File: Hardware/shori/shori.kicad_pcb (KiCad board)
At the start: 4 copper layers, 106 x 44.5 mm, 130 parts, among them J2 SWD_Header, SW1 SW_SPDT, U1 CS4272, U2 STM32H750VBTx, U3 NE5532, U4 NE5532, U5 TPS73733DCQR, U6 W25Q128JVS, U7 TLV9001IDCK, U8 MAX40200AUK, Y1 16MHz

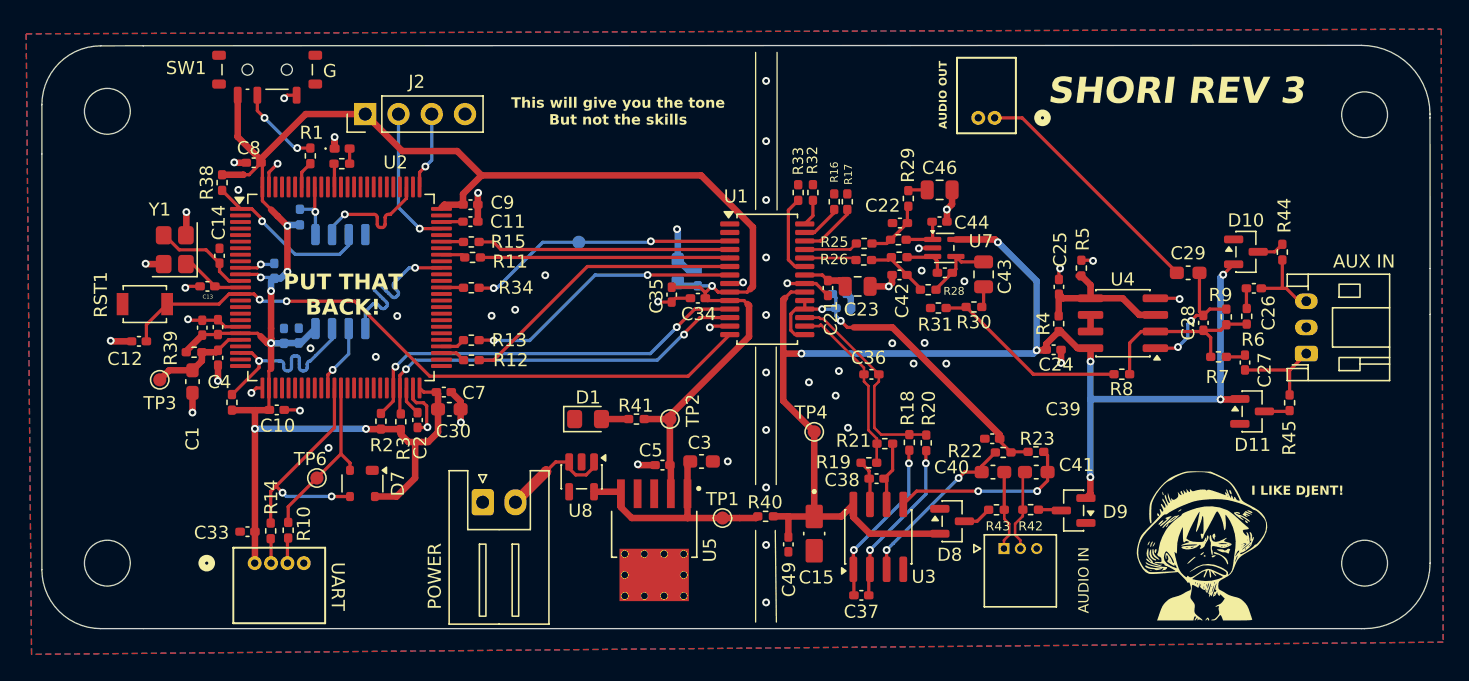
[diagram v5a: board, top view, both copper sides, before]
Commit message: Mae rev 1 schems done! power supply and audio out
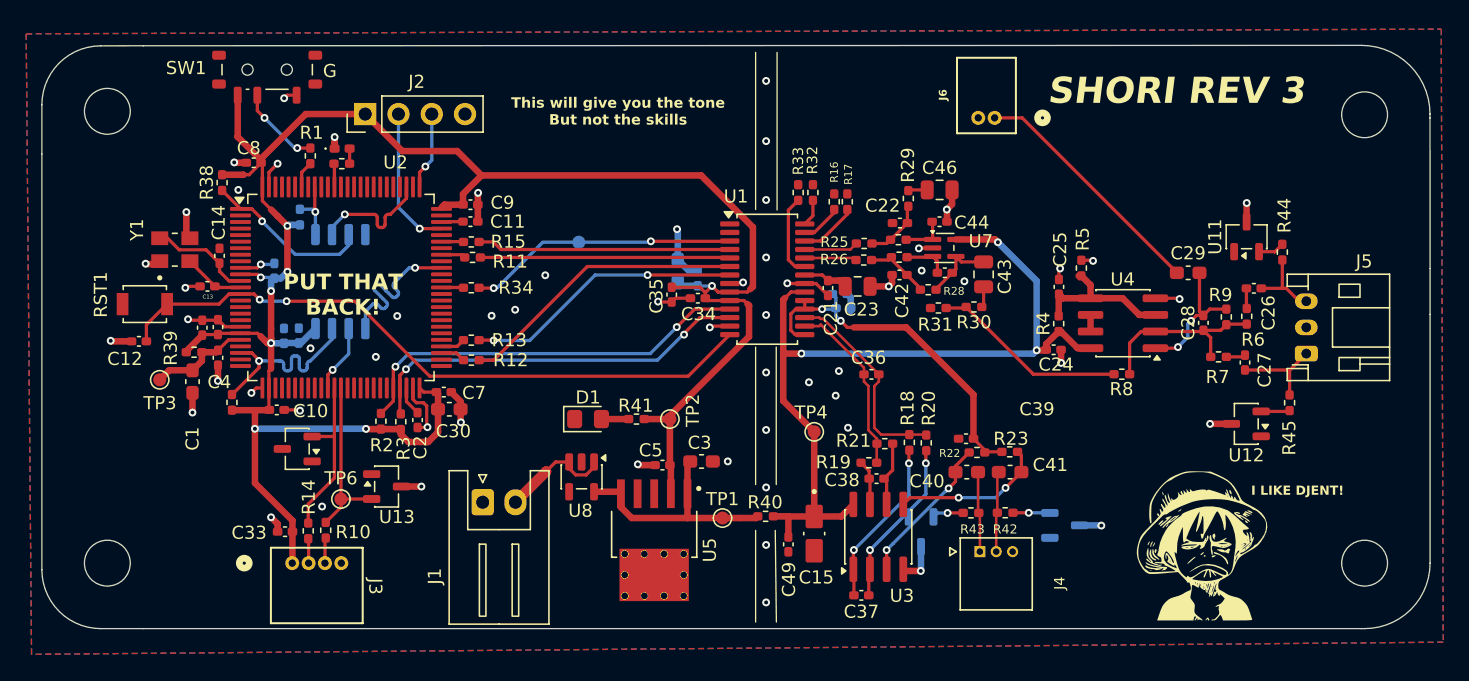
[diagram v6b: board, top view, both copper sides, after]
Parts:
- removed D10, D11, D8, D9: BAT54C, Package_TO_SOT_SMD:SOT-23
- removed D7: PRTR5V0U2X, Package_TO_SOT_SMD:SOT-143
- added U10: ~, Package_TO_SOT_SMD:SOT-23-3, B.Cu at (175.1, 127.6)
- added U11: ~, Package_TO_SOT_SMD:SOT-23-3, F.Cu at (189.0, 105.6)
- added U12: ~, Package_TO_SOT_SMD:SOT-23-3, F.Cu at (189.0, 119.9)
- added U13: ~, Package_TO_SOT_SMD:SOT-23-3, F.Cu at (123.3, 124.7)
- added U14: ~, Package_TO_SOT_SMD:SOT-23-3, F.Cu at (116.5, 121.8)
- added U9: ~, Package_TO_SOT_SMD:SOT-23-3, B.Cu at (164.1, 128.1)
- J4: renamed from AUDIO IN
- J5: renamed from AUX IN
- J6: renamed from AUDIO OUT
- Y1: footprint Crystal:Crystal_SMD_3225-4Pin_3.2x2.5mm -> MyFootprints:XTAL_ABM8-12.288MHZ-B2-T
- moved C33 2.87 mm to (115.6, 128.1)
- moved J3 2.87 mm to (116.1, 130.5)
- moved R10 2.87 mm to (118.7, 128.0)
- moved R14 2.87 mm to (117.3, 128.0)
- moved TP6 2.44 mm to (119.8, 125.6)
- moved C39 2.00 mm to (167.6, 121.0)
- moved C40 2.00 mm to (167.6, 123.5)
- moved C41 2.00 mm to (170.9, 123.5)
- moved R22 2.00 mm to (168.4, 122.0)
- moved R23 2.00 mm to (170.9, 122.0)
- moved R43 1.96 mm to (167.9, 126.7)
- moved R42 1.96 mm to (170.6, 126.7)
- moved J4 1.86 mm to (168.6, 129.6)
- renumbered POWER to J1, UART to J3
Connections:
- R42 pad 1: Net-(D9-Pad3) -> /SHUNT_RES_AINM
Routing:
- net +5VA: track 107.1 -> 65.2 mm, vias 7 -> 3
- net GND: track 58.1 -> 65.9 mm, vias 59 -> 61
- net /UART_RX_RES: track 18.3 -> 12.8 mm, vias 2 -> 0
- net +3.3V: track 169.8 -> 164.6 mm
- net /SHUNT_RES_AINM: track 0.00 -> 2.82 mm, vias 0 -> 1
- net Net-(U3B-+): track 14.1 -> 11.7 mm
- net Net-(D9-Pad3): track 1.77 -> 0.00 mm
- net /LOAD_CAP14: track 7.73 -> 9.41 mm, vias 0 -> 1
- net Net-(U3A-+): track 13.1 -> 11.5 mm, vias 2 -> 1
- net /LOAD_CAP13: track 4.54 -> 5.91 mm, vias 0 -> 1

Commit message: shori final touches!
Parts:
- removed the G*** at (149.0, 113.0)
- added C50: 10uF, Capacitor_SMD:C_0603_1608Metric_Pad1.08x0.95mm_HandSolder, B.Cu at (171.5, 111.8)
- added C51: 10uF, Capacitor_SMD:C_0603_1608Metric_Pad1.08x0.95mm_HandSolder, F.Cu at (177.5, 107.5)
- added G***: LOGO, MyFootprints:logo, F.Cu at (155.9, 93.0)
- added GND: GROUND PROBE, Connector_PinSocket_2.00mm:PinSocket_1x02_P2.00mm_Vertical, F.Cu at (101.8, 121.8)
- AUDIO IN: renamed from J4
- AUDIO OUT: renamed from J6
- AUX IN: renamed from J5
- Y1: footprint MyFootprints:XTAL_ABM8-12.288MHZ-B2-T -> Crystal:Crystal_SMD_3225-4Pin_3.2x2.5mm_HandSoldering
- moved AUDIO OUT 13.9 mm to (183.7, 96.0)
- moved U9 1.96 mm to (165.4, 129.6)
- moved R5 1.31 mm to (177.4, 108.8), turned to 180 degrees
- moved Y1 0.94 mm to (106.6, 105.8)
- moved H2 0.38 mm to (197.8, 96.0)
- moved H4 0.25 mm to (102.0, 95.8)
- renumbered TP2 to 3V3, TP3 to 3V3A, TP1 to 5V, TP4 to 5VA, TP5 to MCK, SW1 to P, J1 to POWER, J2 to PROGRAMMING, RST1 to RST, TP6 to TX, J3 to UART
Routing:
- net /AUDIO_OUT: track 18.8 -> 12.4 mm
- net GND: track 65.9 -> 68.6 mm, vias 61 -> 121
- net /CODEC_AIN-: track 13.6 -> 15.8 mm
- net +5VA: track 65.2 -> 66.7 mm
- net /QSPI_IO2: track 13.7 -> 14.7 mm
- net /LOAD_CAP13: track 5.91 -> 4.96 mm, vias 1 -> 0
- net /VBIAS: track 12.0 -> 12.7 mm
- net /LOAD_CAP14: track 9.41 -> 8.98 mm, vias 1 -> 0
- net /SHUNT_RES_AINP: track 2.39 -> 2.54 mm, vias 0 -> 1
- net Net-(U3A-+): vias 1 -> 2
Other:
- board size 106 x 44.5 mm -> 106 x 44.8 mm
- board text added: "WAVE FORGE"
- board text removed: "PUT THAT BACK!"

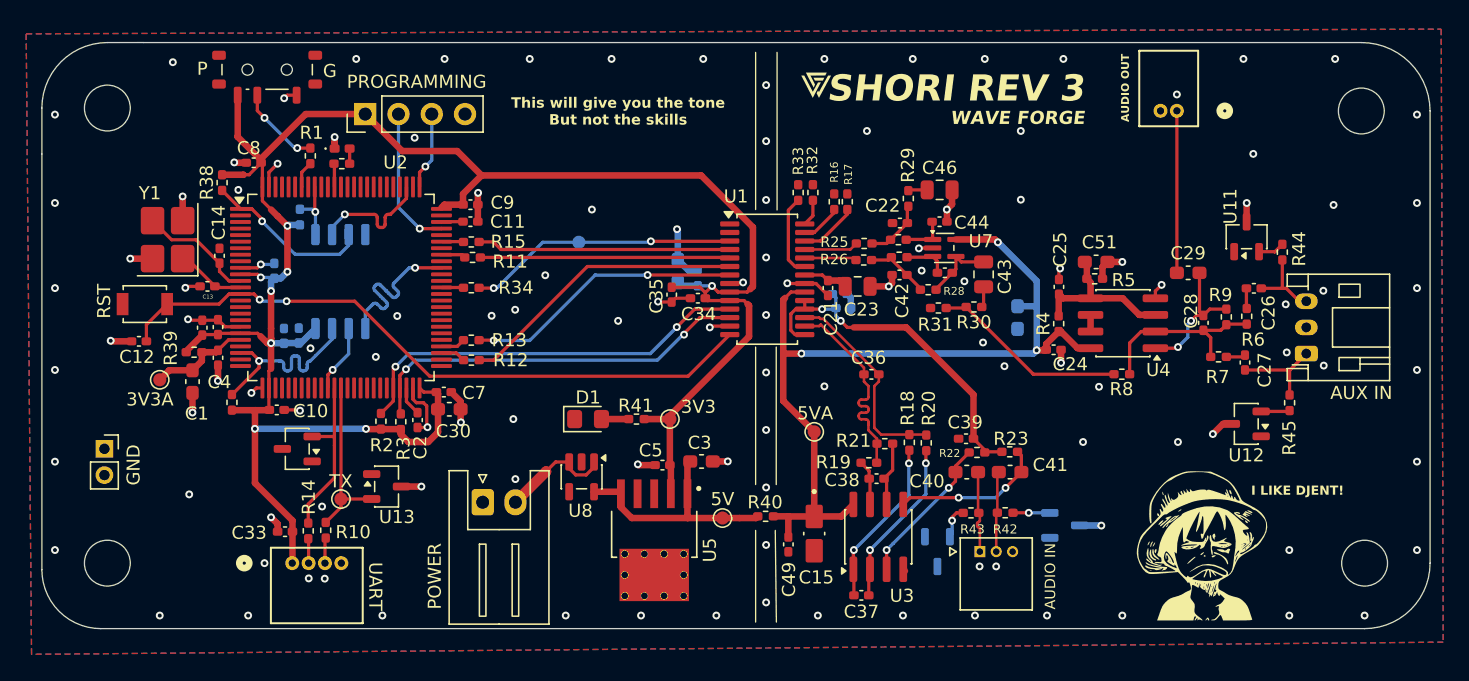
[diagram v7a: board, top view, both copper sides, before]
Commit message: Shori: cleaned up flash and added more BOM
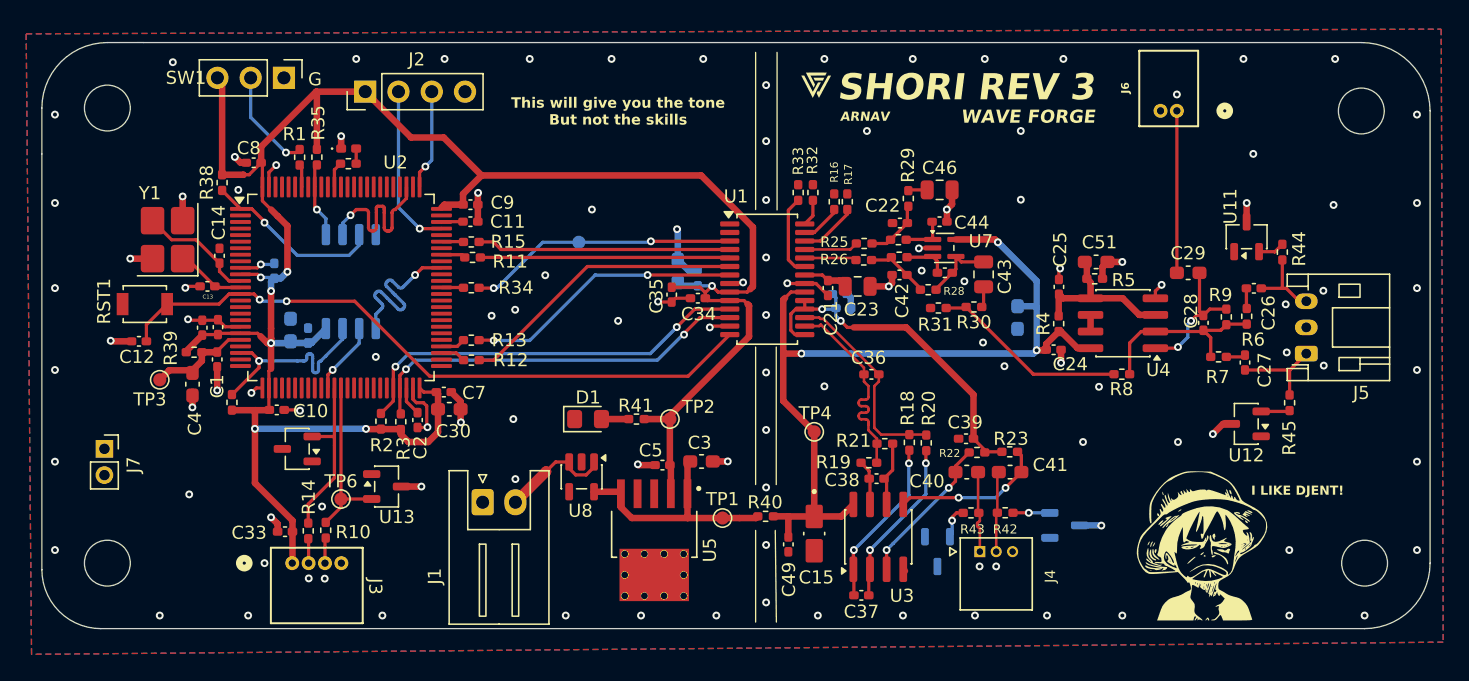
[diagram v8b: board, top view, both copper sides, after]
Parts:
- C1: footprint Capacitor_SMD:C_0603_1608Metric_Pad1.08x0.95mm_HandSolder -> Capacitor_SMD:C_0402_1005Metric_Pad0.74x0.62mm_HandSolder
- C17: value 10μF -> 10uF
- C20: value 0.1uF -> 100nF
- C4, C47: footprint Capacitor_SMD:C_0402_1005Metric_Pad0.74x0.62mm_HandSolder -> Capacitor_SMD:C_0603_1608Metric_Pad1.08x0.95mm_HandSolder
- J4: renamed from AUDIO IN
- J5: renamed from AUX IN
- J6: renamed from AUDIO OUT
- R35: moved to F.Cu
- SW1: renamed from P; footprint Button_Switch_SMD:SW_SPDT_Shouhan_MSK12C02 -> Connector_PinHeader_2.54mm:PinHeader_1x03_P2.54mm_Vertical
- moved R35 4.76 mm to (118.0, 99.5), turned to 90 degrees
- moved C4 2.81 mm to (108.5, 116.8)
- moved C1 2.53 mm to (110.4, 114.9)
- moved J2 1.71 mm to (121.7, 94.5)
- moved SW1 1.42 mm to (115.5, 93.4), turned to -90 degrees
- moved R1 0.82 mm to (116.7, 99.5)
- moved U6 0.80 mm to (120.6, 109.0)
- moved C48 0.71 mm to (117.3, 113.1)
- moved C47 0.67 mm to (116.0, 112.7)
- moved D2 0.50 mm to (120.4, 98.8)
- moved R36 0.50 mm to (120.4, 100.0)
- renumbered POWER to J1, PROGRAMMING to J2, UART to J3, GND to J7, RST to RST1, 5V to TP1, 3V3 to TP2, 3V3A to TP3, 5VA to TP4, MCK to TP5, TX to TP6
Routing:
- net +3.3V: track 164.6 -> 172.6 mm, vias 8 -> 7
- net /QSPI_IO1: track 9.58 -> 13.6 mm
- net /SWDIO: track 11.1 -> 12.8 mm
- net /SWCLK: track 5.95 -> 7.66 mm
- net /BOOT0_R_TO_SW: track 6.41 -> 7.97 mm, vias 2 -> 1
- net /QSPI_IO2: track 14.7 -> 13.7 mm
- net GND: track 68.6 -> 67.6 mm, vias 121 -> 117
- net /QSPI_NCS: track 4.92 -> 5.74 mm
- net /QSPI_IO0: track 12.8 -> 13.6 mm
- net /QSPI_IO3: track 16.0 -> 15.4 mm
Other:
- board text added: "ARNAV"
